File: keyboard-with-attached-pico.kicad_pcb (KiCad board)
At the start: 2 copper layers, 233.1 x 85.6 mm, 95 parts

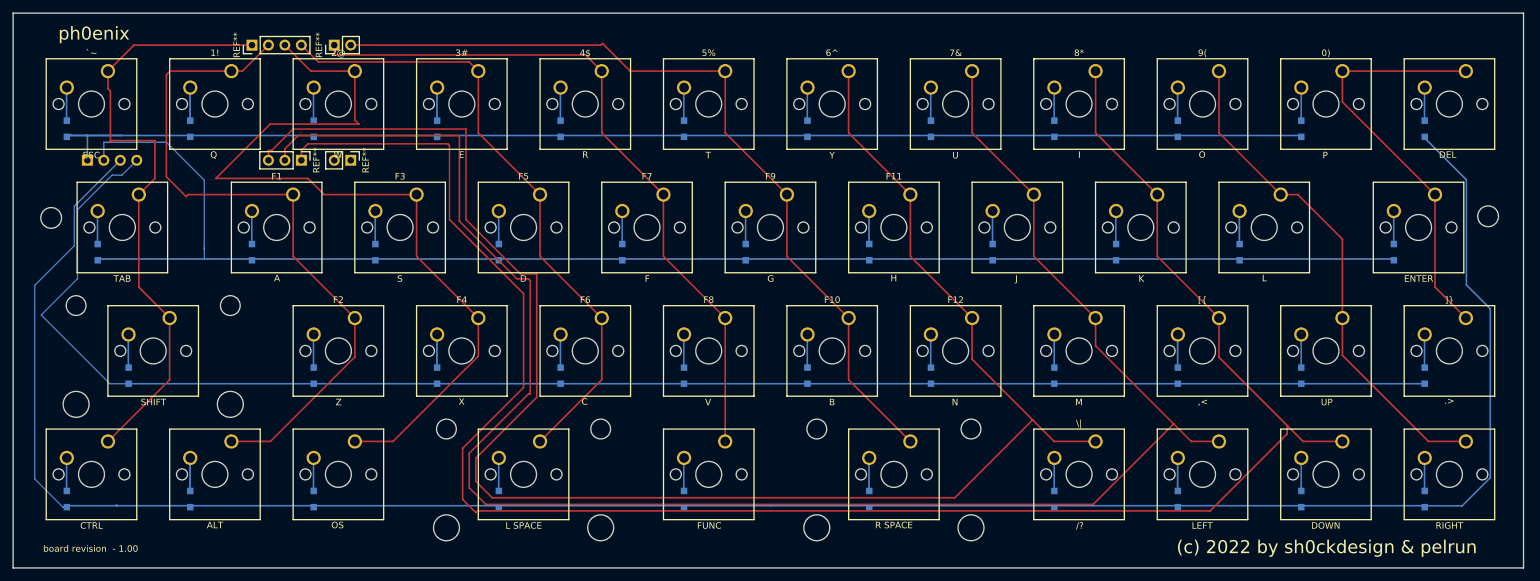
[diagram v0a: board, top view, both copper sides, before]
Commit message: Added new board, and firmware to match
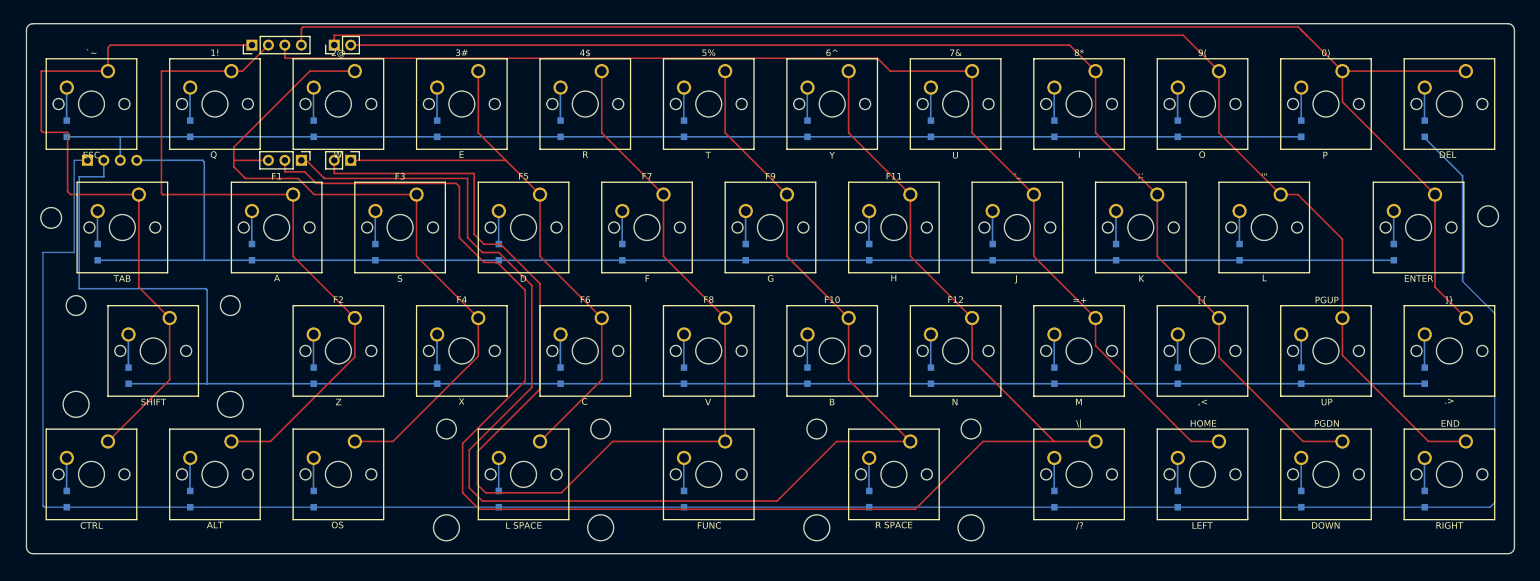
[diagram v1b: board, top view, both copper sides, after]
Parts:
- added G***: LOGO, Graphics:Dither, B.Cu at (147.1, 153.9)
- added G***: LOGO, Graphics:Dither, B.Cu at (277.1, 150.9)
- added G***: LOGO, Graphics:ph0enix, B.Cu at (208.3, 152.1)
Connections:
- D10 pad 1: (no net) -> /Row_0
- REF** pad 1: /Col_4 -> /Col_9
- REF** pad 2: /Col_5 -> /Col_8
- REF** pad 3: /Col_2 -> /Col_7
- REF** pad 4: /Col_3 -> /Col_10
- REF** pad 1: /Col_8 -> /Col_5
- REF** pad 2: /Col_7 -> /Col_6
- REF** pad 3: /Col_6 -> /Col_2
- REF** pad 1: /Col_10 -> /Col_3
- REF** pad 2: /Col_9 -> /Col_4
- REF** pad 1: (no net) -> /Row_3
- REF** pad 2: /Row_1 -> /Row_2
- REF** pad 3: /Row_3 -> /Row_0
- REF** pad 4: /Row_2 -> /Row_1
- locked pad 1: (no net) -> /Row_0
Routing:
- net /Col_10: track 65.0 -> 232.5 mm
- net /Col_9: track 77.9 -> 218.2 mm
- net /Col_8: track 299.0 -> 193.1 mm
- net /Col_7: track 283.9 -> 184.3 mm
- net /Col_5: track 128.6 -> 225.9 mm
- net /Col_4: track 108.7 -> 188.4 mm
- net /Col_0: track 95.4 -> 114.0 mm
- net /Col_2: track 131.9 -> 115.3 mm
- net /Row_2: track 248.7 -> 257.9 mm
- net /Row_1: track 233.5 -> 225.7 mm
- net /Col_6: track 266.3 -> 259.6 mm
- net /Row_3: track 340.0 -> 345.5 mm
- net /Col_3: track 98.0 -> 93.1 mm
- net /Row_0: track 198.5 -> 194.2 mm
- net (no net): track 3.82 -> 0.00 mm
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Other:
- board size 233.1 x 85.6 mm -> 229.6 x 81.8 mm
- board text added: "'{dblquote}"
- board text added: "-_"
- board text added: ";:"
- board text added: "=+"
- board text added: "END"
- board text added: "HOME"
- board text added: "PGDN"
- board text added: "PGUP"
- board text added: "board revision - 1.01"
- board text removed: "board revision - 1.00"

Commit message: Minor position change on the Phoenix graphic and removal of D5 text
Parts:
- moved G*** 1.02 mm to (209.3, 152.1)
